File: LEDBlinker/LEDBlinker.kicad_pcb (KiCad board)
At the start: 2 copper layers, 83 x 38 mm, 26 parts, among them J1 USB-C Breakout, SW1 SW_SPDT, U1 LM555xN, U2 CD4017BE

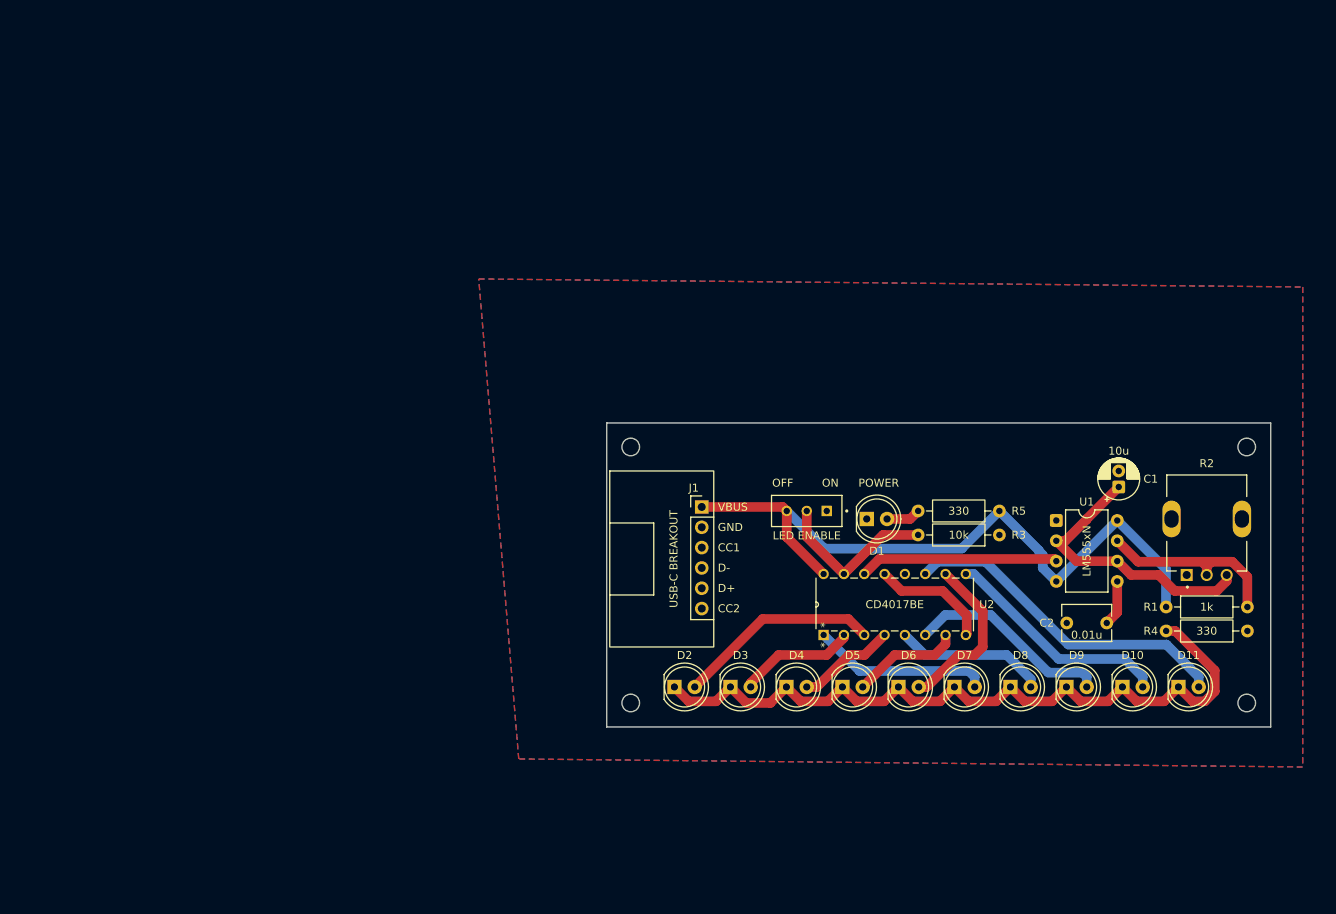
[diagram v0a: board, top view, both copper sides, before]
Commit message: Created PCB in shape of SMEE
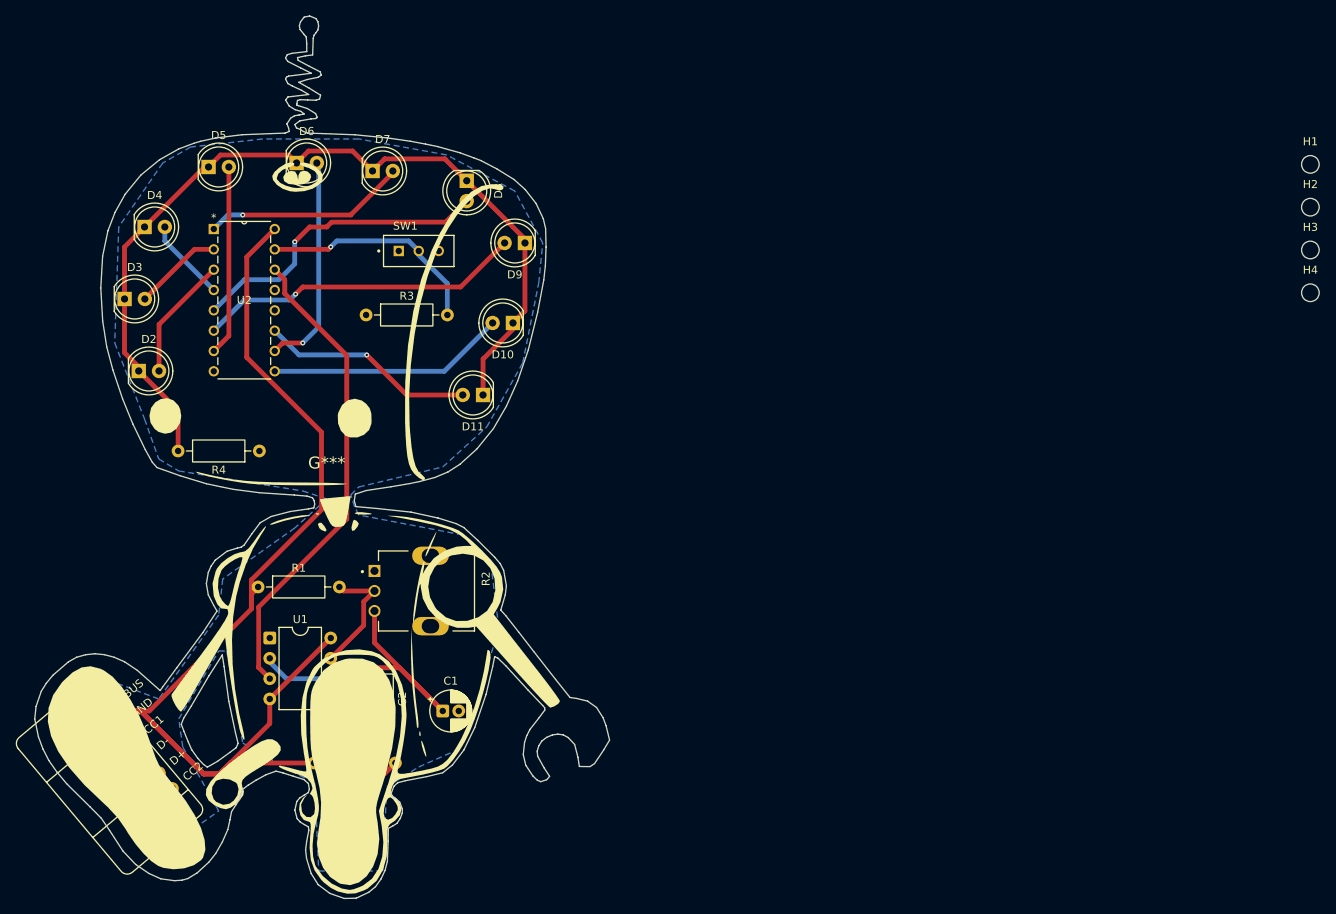
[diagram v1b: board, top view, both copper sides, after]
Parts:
- added G***: LOGO, LOGO, F.Cu at (64.5, 85.0)
- moved R4 125.5 mm to (56.1, 83.5)
- moved R1 113.5 mm to (55.9, 100.5)
- moved D5 102.5 mm to (49.7, 48.0)
- moved H3 102.1 mm to (187.5, 58.4)
- moved D6 99.8 mm to (60.7, 47.5)
- moved U1 99.4 mm to (57.4, 106.9)
- moved D4 98.7 mm to (41.7, 55.5)
- moved R2 97.4 mm to (77.5, 101.0), turned to -90 degrees
- moved D7 97.2 mm to (70.2, 48.5)
- moved D11 94.3 mm to (84.0, 76.5), turned to 180 degrees
- moved D8 92.9 mm to (82.0, 49.7), turned to -90 degrees
- moved H1 92.0 mm to (187.5, 47.7)
- moved C2 91.8 mm to (70.5, 112.0), turned to -90 degrees
- moved R5 91.3 mm to (62.9, 122.5), turned to 0 degrees
- moved U2 90.0 mm to (58.0, 73.5), turned to 0 degrees
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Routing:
- net +5V: track 87.0 -> 152.9 mm
- net /OUT: track 24.9 -> 60.0 mm
- net Net-(D8-A): track 19.0 -> 38.9 mm, vias 0 -> 1
- net Net-(D10-K): track 93.2 -> 111.6 mm
- net Net-(D11-A): track 42.1 -> 26.8 mm, vias 0 -> 1
- net Net-(D9-A): track 25.7 -> 40.9 mm, vias 0 -> 1
- net GND: track 14.9 -> 0.00 mm
- net Net-(D5-A): track 13.7 -> 23.8 mm
- net Net-(D2-A): track 25.5 -> 15.5 mm
- net Net-(U1-DISCH): track 24.6 -> 15.3 mm
- net Net-(D1-A): track 4.29 -> 11.8 mm
- net Net-(SW1-B): track 21.1 -> 28.4 mm, vias 0 -> 1
- net Net-(D6-A): track 21.1 -> 27.5 mm, vias 0 -> 1
- net Net-(U1-THRES): track 35.8 -> 41.8 mm
- net Net-(D3-A): track 14.8 -> 11.2 mm
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- removed copper zone on F.Cu, net GND
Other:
- board size 83 x 38 mm -> 71.9 x 110.3 mm
- board text removed: "LED ENABLE"
- board text removed: "OFF"
- board text removed: "ON"
- board text removed: "POWER"
